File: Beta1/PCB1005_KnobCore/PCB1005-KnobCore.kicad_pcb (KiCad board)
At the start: 2 copper layers, 160 x 60.2 mm, 45 parts, among them J1 Axoloti_40Pin, U10 OLED_128x32_I2C, U1000 MCP3008T-I/SL, U2 MCP3008T-I/SL, U20 OLED_128x32_I2C, U30 OLED_128x32_I2C, U40 OLED_128x32_I2C, U5 I2C_1x4MUX_TCA9546A

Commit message: Routed
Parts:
- removed C1, C1000: 0.1u, Capacitors_SMD:C_0603
- removed RC0, RC10, RC20, RC30, RC40, RD0, RD10, RD20, RD30, RD40, RR0: 10K, Resistors_SMD:R_0603
- removed RV0, RV1, RV2, RV3, RV4, RV5, RV6, RV7: POT, Liberry:RV09AF-40-20K-B10K
- removed U10, U20, U30, U40: OLED_128x32_I2C, Liberry:OLED_128x32
- removed U1000: MCP3008T-I/SL, Liberry:SOIC-16
- removed U5: I2C_1x4MUX_TCA9546A, Liberry:SOIC-16_1.27x5.4
- added J10: CON_1x4, Liberry:CON_0.1_x4_Double, F.Cu at (11.4, -58.9)
- added J11: CON_1x4, Liberry:CON_0.1_x4_Double, F.Cu at (148.6, -51.3)
- added J20: CON_1x4, Liberry:CON_0.1_x4_Double_Joy_symbol, F.Cu at (134.3, -38.8)
- added J21: CON_1x4, Liberry:CON_0.1_x4_Double_Joy_symbol, F.Cu at (16.2, -38.8)
- added REF**: 1pin, Connect:1pin, F.Cu at (3.50, -52.2)
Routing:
- net GND: track 475.0 -> 7.45 mm, vias 10 -> 0
- net +3V3: track 623.0 -> 349.0 mm, vias 7 -> 0
- net /I2C_SDA3: track 104.9 -> 0.00 mm, vias 2 -> 0
- net /I2C_SCL3: track 103.0 -> 0.00 mm, vias 2 -> 0
- net /P0: track 80.3 -> 0.00 mm, vias 1 -> 0
- net /!OLED_RESET: track 71.2 -> 0.00 mm, vias 3 -> 0
- net /I2C_SDA2: track 68.0 -> 0.00 mm, vias 2 -> 0
- net /P7: track 65.4 -> 0.00 mm
- net /I2C_SCL2: track 64.7 -> 0.00 mm, vias 2 -> 0
- net /I2C_SDA0: track 63.9 -> 0.00 mm
- net /P1: track 59.1 -> 0.00 mm, vias 1 -> 0
- net /I2C_SCL0: track 48.6 -> 0.00 mm
- net /P6: track 44.8 -> 0.00 mm
- net /CS_8_15: track 84.1 -> 127.7 mm, vias 3 -> 2
- net /I2C_SDA: track 43.0 -> 85.2 mm
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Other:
- board text added: "PCB1005_KnobCore_2017-08-01 github.com/Believotron/BelievotronWanderlustHardware"
- board text removed: "PCB1005_KnobCore_2017-07-17 github.com/Believotron/BelievotronWanderlustHardware"
- board text removed: "RV09AF-40-20K-B10K"
- board text removed: "TCA9546ADR"

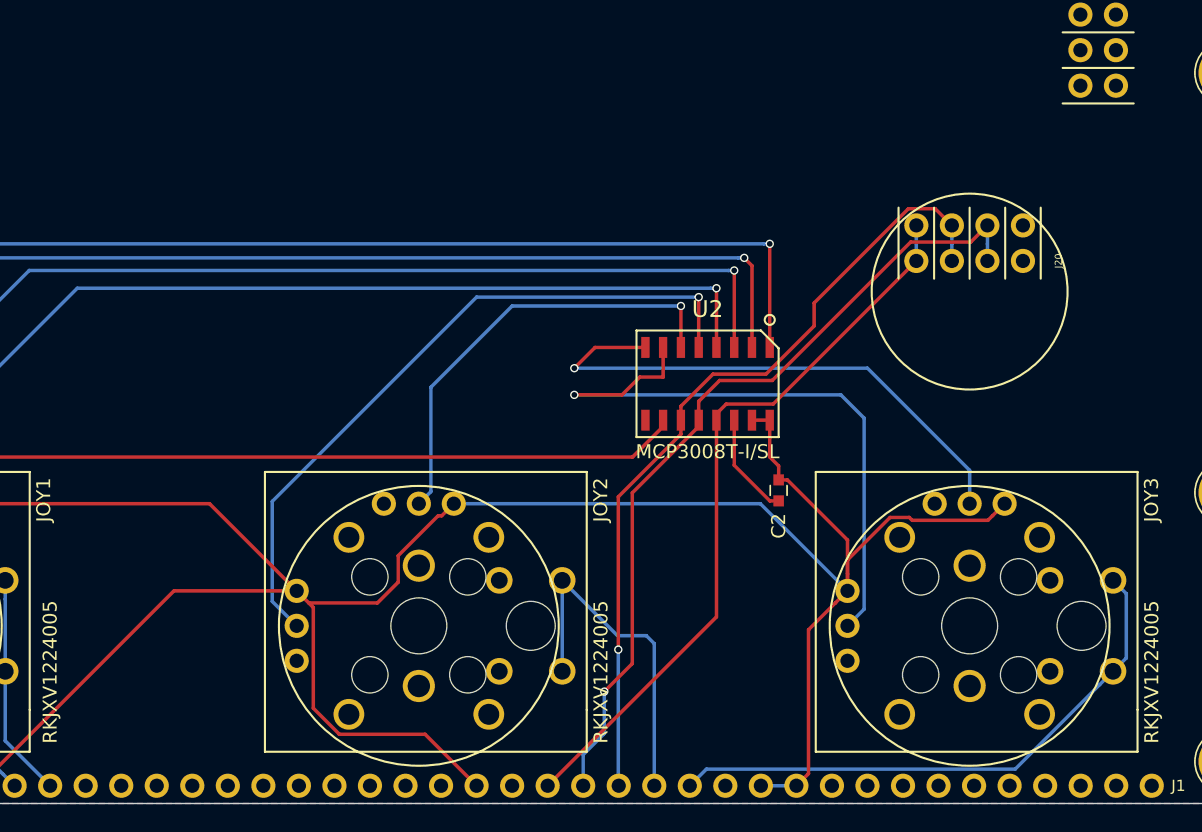
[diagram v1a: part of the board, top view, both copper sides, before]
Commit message: Added !OLED_RESET
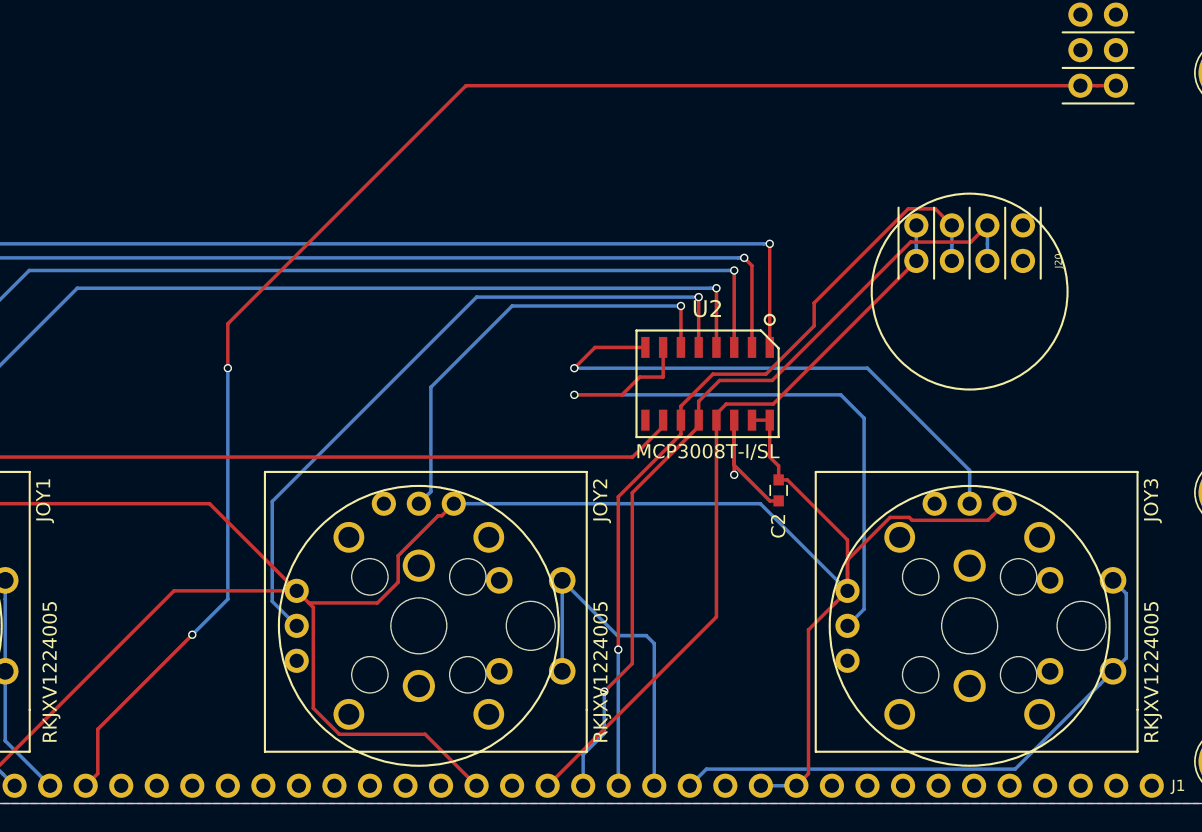
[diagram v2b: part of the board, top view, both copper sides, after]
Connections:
- J11 pad 1: GND -> /!OLED_RESET
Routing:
- net /!OLED_RESET: track 0.00 -> 107.8 mm, vias 0 -> 2
- net GND: track 7.45 -> 11.4 mm, vias 0 -> 1
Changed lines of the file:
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@@
     (thickness 1.6)
     (drawings 23)
-    (tracks 245)
+    (tracks 259)
     (zones 0)
     (modules 23)
@@
     (fp_line (start 8.89 -3.81) (end 8.89 1.27) (layer F.SilkS) (width 0.15))
     (pad 1 thru_hole circle (at 0 -2.54) (size 1.7272 1.7272) (drill 1.016) (layers *.Cu *.Mask)
-      (net 1 GND))
+      (net 23 /!OLED_RESET))
     (pad 1 thru_hole circle (at 0 0) (size 1.7272 1.7272) (drill 1.016) (layers *.Cu *.Mask)
-      (net 1 GND))
+      (net 23 /!OLED_RESET))
     (pad 2 thru_hole circle (at 2.54 -2.54) (size 1.7272 1.7272) (drill 1.016) (layers *.Cu *.Mask)
       (net 1 GND))
@@
   (gr_line (start 0 0) (end 0 -60.22) (layer Edge.Cuts) (width 0.1))
   (gr_line (start 0 0) (end 160 0) (layer Edge.Cuts) (width 0.1))
+  (via (at 121.285 -23.495) (size 0.6) (drill 0.4) (layers F.Cu B.Cu) (net 1))
+  (segment (start 121.285 -27.4) (end 121.285 -23.495) (width 0.25) (layer F.Cu) (net 1))
   (segment (start 121.285 -27.4) (end 121.285 -24.18) (width 0.25) (layer F.Cu) (net 1))
   (segment (start 123.835 -21.63) (end 124.46 -21.63) (width 0.25) (layer F.Cu) (net 1))
@@
   (segment (start 18.7325 -38.782) (end 18.7325 -40.003314) (width 0.25) (layer B.Cu) (net 18))
   (segment (start 18.7325 -40.003314) (end 18.7325 -41.322) (width 0.25) (layer B.Cu) (net 18))
+  (segment (start 146.03 -51.308) (end 147.251314 -51.308) (width 0.25) (layer F.Cu) (net 23))
+  (segment (start 147.251314 -51.308) (end 148.57 -51.308) (width 0.25) (layer F.Cu) (net 23))
+  (segment (start 85.09 -34.29) (end 102.108 -51.308) (width 0.25) (layer F.Cu) (net 23))
+  (segment (start 102.108 -51.308) (end 146.03 -51.308) (width 0.25) (layer F.Cu) (net 23))
+  (segment (start 85.09 -31.115) (end 85.09 -34.29) (width 0.25) (layer F.Cu) (net 23))
+  (segment (start 85.09 -14.605) (end 85.09 -31.115) (width 0.25) (layer B.Cu) (net 23))
+  (via (at 85.09 -31.115) (size 0.6) (drill 0.4) (layers F.Cu B.Cu) (net 23))
+  (segment (start 82.55 -12.065) (end 85.09 -14.605) (width 0.25) (layer B.Cu) (net 23))
+  (segment (start 75.793599 -5.308599) (end 82.55 -12.065) (width 0.25) (layer F.Cu) (net 23))
+  (via (at 82.55 -12.065) (size 0.6) (drill 0.4) (layers F.Cu B.Cu) (net 23))
+  (segment (start 74.93 -1.27) (end 75.793599 -2.133599) (width 0.25) (layer F.Cu) (net 23))
+  (segment (start 75.793599 -2.133599) (end 75.793599 -5.308599) (width 0.25) (layer F.Cu) (net 23))
   (segment (start 30.2525 -15.95) (end 30.2525 -14.606498) (width 0.25) (layer B.Cu) (net 24))
   (segment (start 30.2525 -14.606498) (end 30.2525 -9.45) (width 0.25) (layer B.Cu) (net 24))

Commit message: Finished routing
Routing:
- net /CS_8_15: track 127.7 -> 128.2 mm
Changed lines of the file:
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@@
   (general
     (links 93)
-    (no_connects 1)
+    (no_connects 0)
     (area -0.050001 -60.270001 160.050001 0.050001)
     (thickness 1.6)
@@
     (34 B.Paste user)
     (35 F.Paste user)
-    (36 B.SilkS user hide)
+    (36 B.SilkS user)
     (37 F.SilkS user)
     (38 B.Mask user)
@@
     (effects (font (size 1 1) (thickness 0.15)) (justify left))
   )
-  (gr_text "Open source MIT license files at: github.com/Believotron/BelievotronWanderlustHardware\nReplacement parts, upgrades, updates, new gear, and marketing pap: Believotron.com\nFor help, bug reporting, dev-blogs, or joy at your bonkers-cool creation, \nthe good stuff is here: community.believotron.com\n" (at 49.784 -3.302) (layer B.SilkS)
+  (gr_text "Open source MIT license files at: github.com/Believotron/BelievotronWanderlustHardware\nReplacement parts, upgrades, updates, new gear, and marketing pap: Believotron.com\nFor help, bug reporting, dev-blogs, or joy at your bonkers-cool creation, \nthe good stuff is here: community.believotron.com\n" (at 143.51 -56.515) (layer B.SilkS)
     (effects (font (size 0.7 0.7) (thickness 0.15)) (justify left mirror))
   )
@@
   (segment (start 120.015 -27.4) (end 120.015 -13.335) (width 0.25) (layer F.Cu) (net 6))
   (segment (start 120.015 -13.335) (end 107.95 -1.27) (width 0.25) (layer F.Cu) (net 6))
+  (segment (start 118.745 -27.4) (end 118.745 -25.4) (width 0.25) (layer F.Cu) (net 7))
+  (segment (start 118.745 -25.4) (end 114 -20.655) (width 0.25) (layer F.Cu) (net 7))
+  (segment (start 114 -20.655) (end 114 -10) (width 0.25) (layer F.Cu) (net 7))
+  (segment (start 114 -10) (end 112 -8) (width 0.25) (layer F.Cu) (net 7))
   (segment (start 139.3825 -38.782) (end 139.3825 -40.003314) (width 0.25) (layer B.Cu) (net 7))
   (segment (start 139.3825 -40.003314) (end 139.3825 -41.322) (width 0.25) (layer B.Cu) (net 7))
@@
   (segment (start 112 -8) (end 112 -5) (width 0.25) (layer B.Cu) (net 7))
   (via (at 112 -8) (size 0.6) (drill 0.4) (layers F.Cu B.Cu) (net 7))
-  (segment (start 114 -10) (end 112 -8) (width 0.25) (layer F.Cu) (net 7))
-  (segment (start 114 -22.205) (end 114 -10) (width 0.25) (layer F.Cu) (net 7))
-  (segment (start 118.745 -27.4) (end 118.745 -26.95) (width 0.25) (layer F.Cu) (net 7))
-  (segment (start 118.745 -26.95) (end 114 -22.205) (width 0.25) (layer F.Cu) (net 7))
   (segment (start 120.23863 -30.23863) (end 118.745 -28.745) (width 0.25) (layer F.Cu) (net 7))
   (segment (start 118.745 -28.745) (end 118.745 -27.4) (width 0.25) (layer F.Cu) (net 7))
@@
   (segment (start 117.475 -27.4) (end 117.475 -26.4) (width 0.25) (layer F.Cu) (net 8))
   (segment (start 117.475 -26.4) (end 113 -21.925) (width 0.25) (layer F.Cu) (net 8))
+  (segment (start 116.205 -27.4) (end 116.205 -26.035) (width 0.25) (layer F.Cu) (net 17))
+  (segment (start 116.205 -26.035) (end 114.935 -24.765) (width 0.25) (layer F.Cu) (net 17))
+  (segment (start 114.935 -24.765) (end 53.975 -24.765) (width 0.25) (layer F.Cu) (net 17))
+  (segment (start 53.975 -24.765) (end 48.895 -29.845) (width 0.25) (layer F.Cu) (net 17))
   (segment (start 29.21 -26.035004) (end 53.975004 -1.27) (width 0.25) (layer F.Cu) (net 17))
   (segment (start 53.975004 -1.27) (end 54.61 -1.27) (width 0.25) (layer F.Cu) (net 17))
@@
   (segment (start 48.895 -29.845) (end 45.085004 -26.035004) (width 0.25) (layer B.Cu) (net 17))
   (via (at 29.21 -26.035004) (size 0.6) (drill 0.4) (layers F.Cu B.Cu) (net 17))
-  (segment (start 53.975 -24.765) (end 48.895 -29.845) (width 0.25) (layer F.Cu) (net 17))
   (via (at 48.895 -29.845) (size 0.6) (drill 0.4) (layers F.Cu B.Cu) (net 17))
-  (segment (start 114.02 -24.765) (end 53.975 -24.765) (width 0.25) (layer F.Cu) (net 17))
-  (segment (start 116.205 -27.4) (end 116.205 -26.95) (width 0.25) (layer F.Cu) (net 17))
-  (segment (start 116.205 -26.95) (end 114.02 -24.765) (width 0.25) (layer F.Cu) (net 17))
   (segment (start 57.15 -1.27) (end 54.370023 -4.049977) (width 0.25) (layer F.Cu) (net 18))
   (segment (start 54.370023 -4.049977) (end 52.243209 -4.049977) (width 0.25) (layer F.Cu) (net 18))

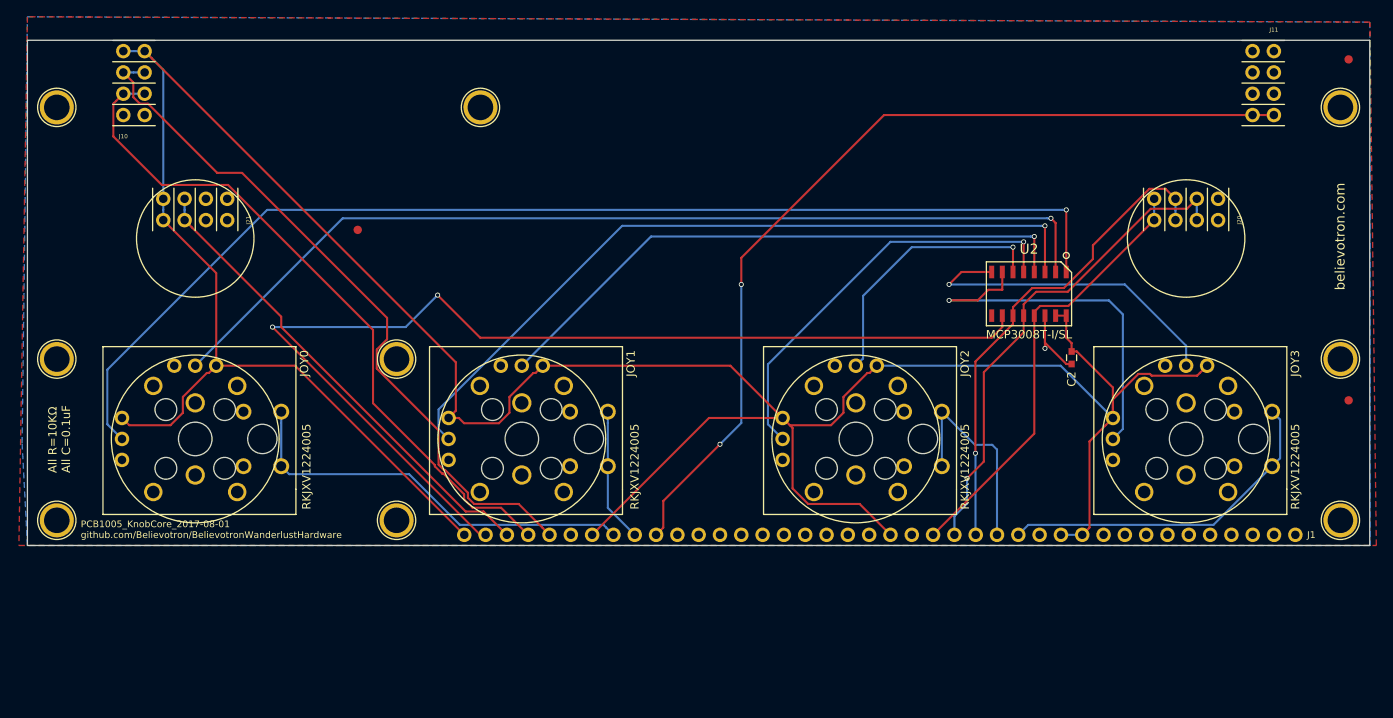
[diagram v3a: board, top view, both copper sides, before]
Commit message: Added FFC connector. Ready for fab
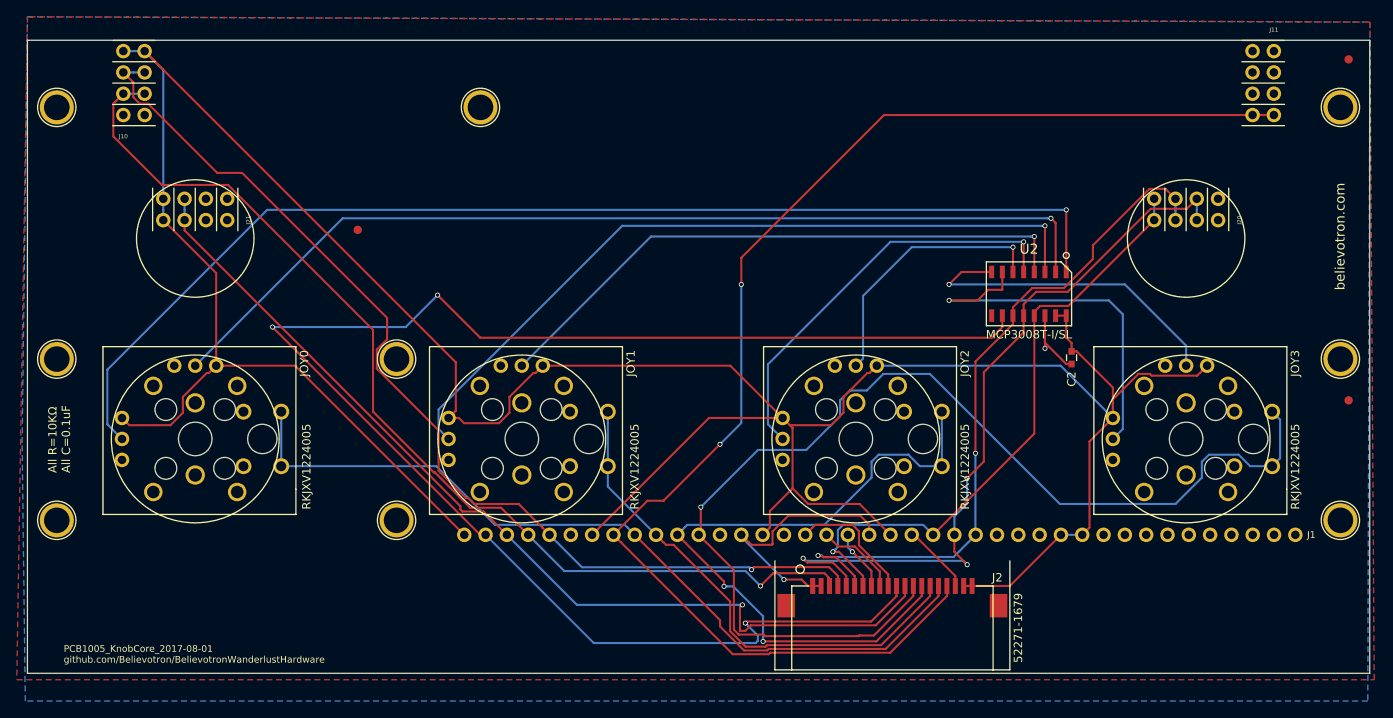
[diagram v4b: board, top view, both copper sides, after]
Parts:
- added J2: FPC_20POS, Liberry:FFC_1MM_20POS_MOLEX_52271-2079, F.Cu at (103.1, 4.83)
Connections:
- J1 pad 10: /!OLED_RESET -> /JOY_1_SW
- J1 pad 11: Net-(J1-Pad11) -> /JOY_2_SW
- J1 pad 12: Net-(J1-Pad12) -> /JOY_3_SW
- J1 pad 15: Net-(J1-Pad15) -> +3V3
- J1 pad 18: Net-(J1-Pad18) -> /TX
- J1 pad 19: Net-(J1-Pad19) -> /RX
- J1 pad 22: Net-(J1-Pad22) -> /ANALOG_OUT
- J1 pad 26: /JOY_2_SW -> Net-(J1-Pad26)
- J1 pad 27: /JOY_3_SW -> Net-(J1-Pad27)
- J1 pad 8: /JOY_0_SW -> /!OLED_RESET
- J1 pad 9: /JOY_1_SW -> /JOY_0_SW
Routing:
- net /JOY_3_SW: track 40.9 -> 134.9 mm, vias 0 -> 1
- net /CS_8_15: track 128.2 -> 189.4 mm, vias 2 -> 3
- net /JOY_2_SW: track 25.1 -> 83.6 mm, vias 0 -> 2
- net /CS_0_7: track 57.2 -> 114.7 mm, vias 0 -> 1
- net /!OLED_RESET: track 107.8 -> 160.7 mm
- net /JOY_0_SW: track 49.5 -> 98.3 mm
- net /JOY_1_SW: track 16.0 -> 61.0 mm
- net /I2C_SCL: track 82.8 -> 123.2 mm, vias 0 -> 1
- net /I2C_SDA: track 85.2 -> 123.1 mm, vias 0 -> 1
- net GND: track 11.4 -> 43.3 mm, vias 1 -> 2
- net /SPI_MISO: track 59.3 -> 90.6 mm, vias 1 -> 3
- net /SPI_MOSI: track 58.2 -> 84.7 mm, vias 1 -> 2
- net +3V3: track 349.0 -> 370.1 mm
- net /SPI_CLK: track 52.9 -> 73.8 mm, vias 0 -> 1
- net /VOLUME: track 0.00 -> 15.2 mm
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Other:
- board size 160 x 60.2 mm -> 160 x 75.5 mm
